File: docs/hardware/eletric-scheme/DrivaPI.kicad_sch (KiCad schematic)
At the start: 0 parts

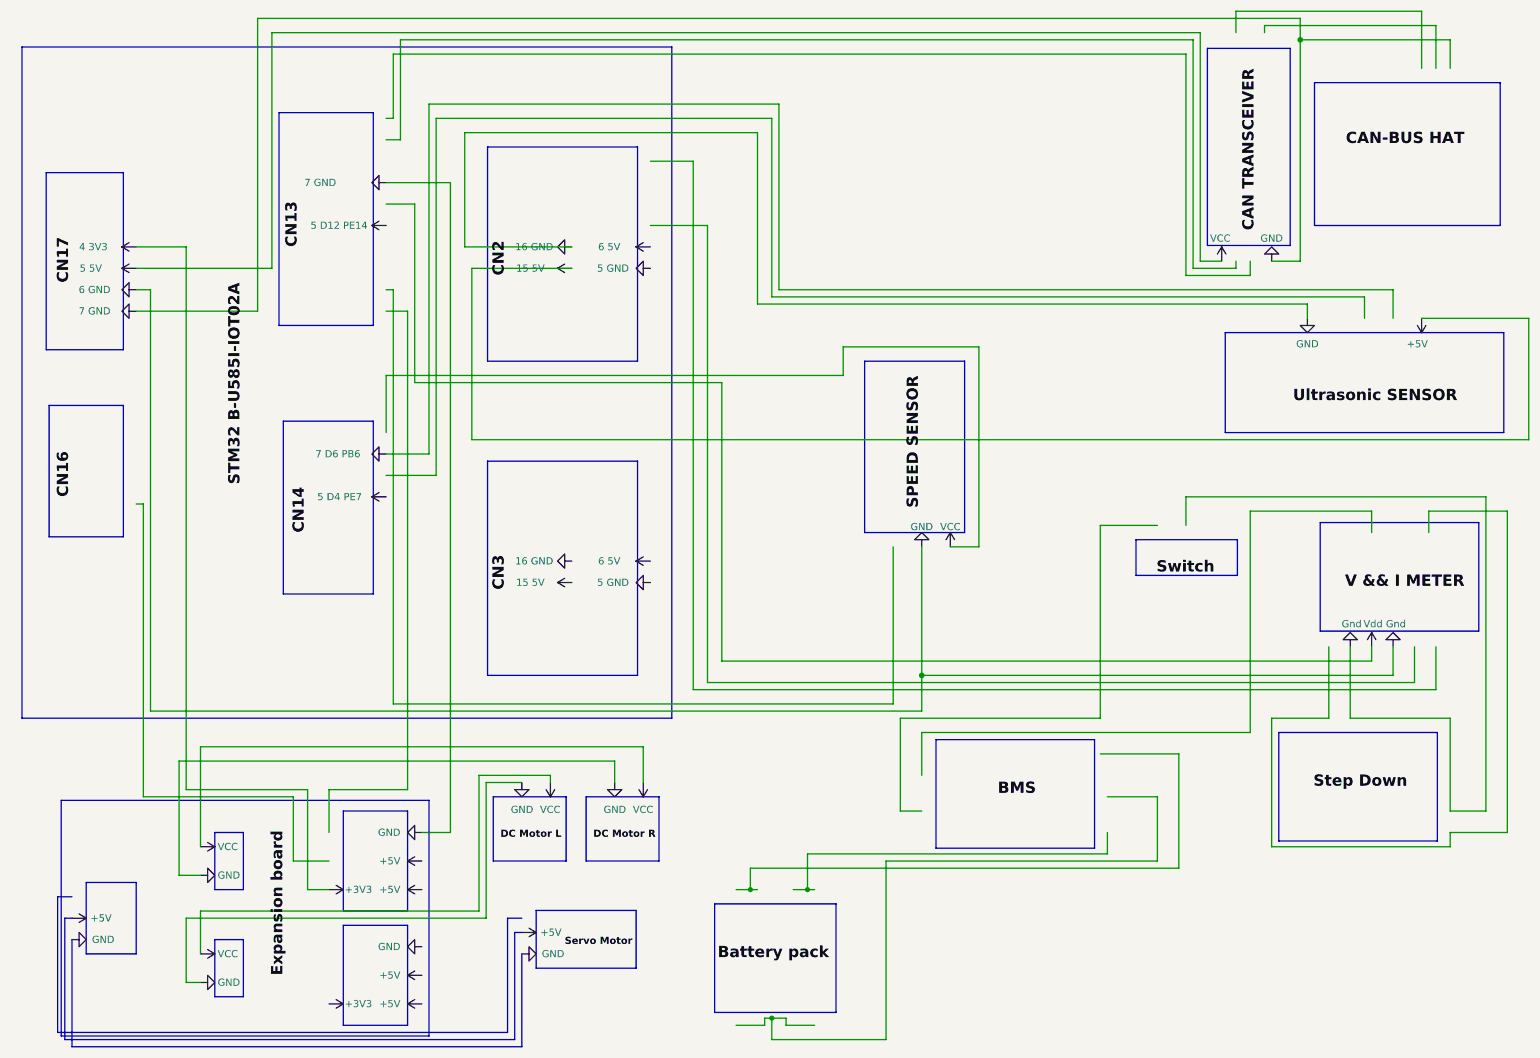
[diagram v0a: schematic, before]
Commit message: update eletric scheme after removing expansion and add abs and h-bridge
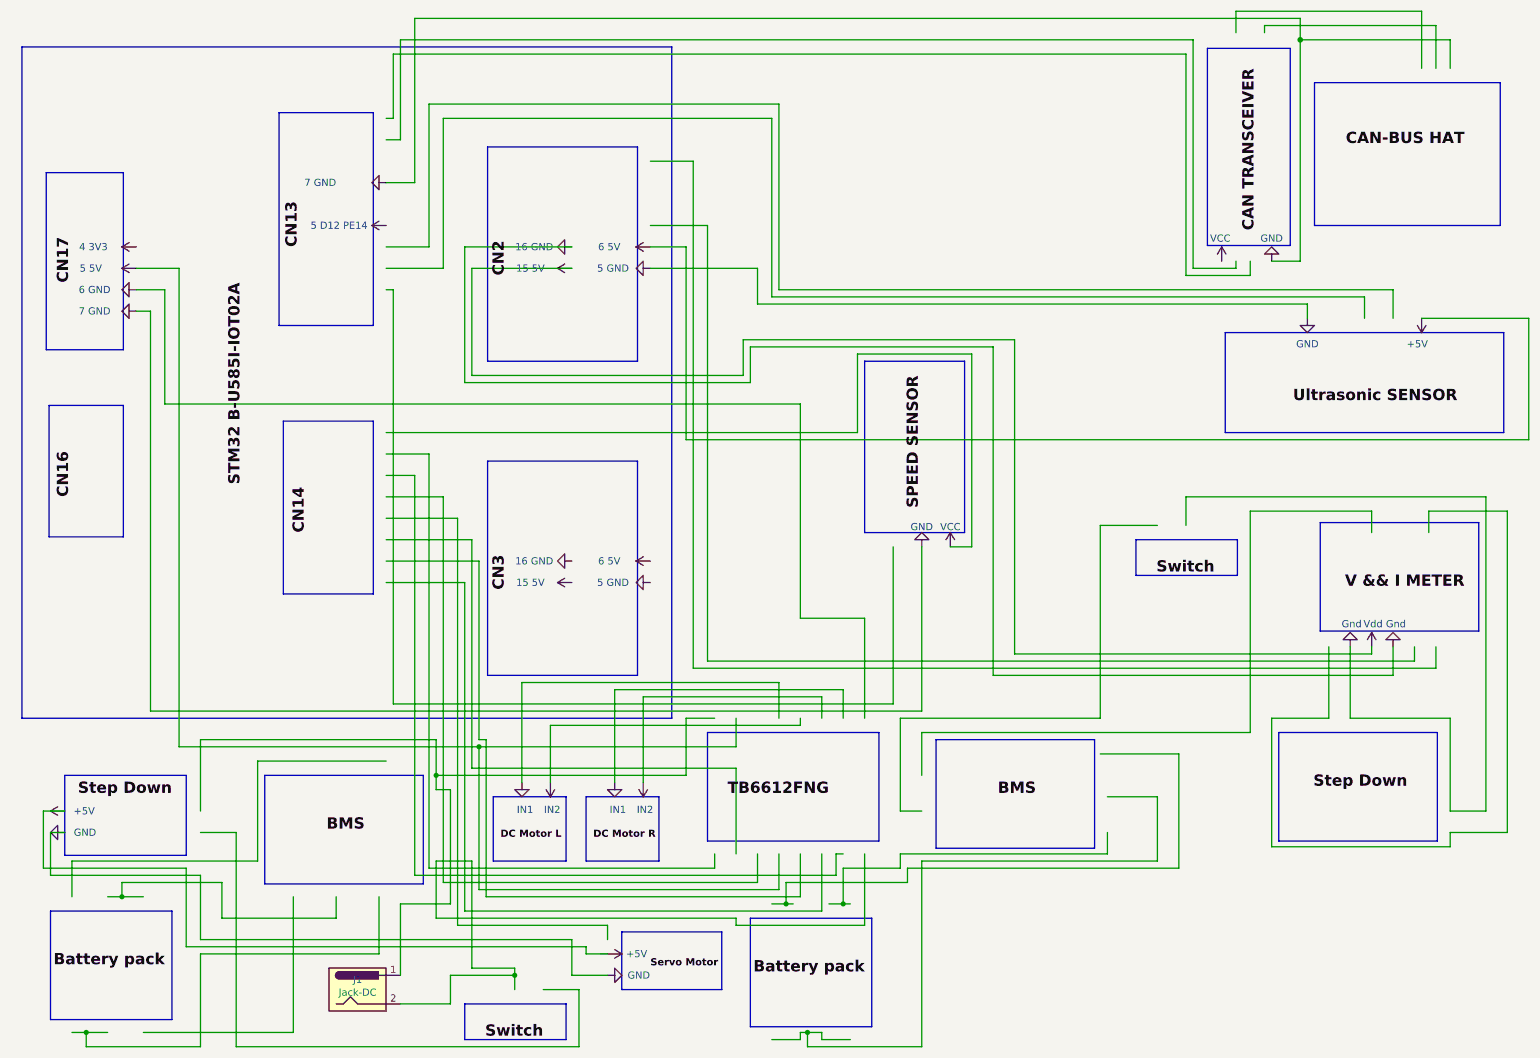
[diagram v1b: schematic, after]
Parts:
- added J1: Jack-DC, symbol Connector:Jack-DC

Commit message: improve eletric scheme
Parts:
- added Capacitor: C_Polarized, symbol Device:C_Polarized
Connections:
- net +5V: now also Capacitor.1
- net 5 GND: now also Capacitor.2
